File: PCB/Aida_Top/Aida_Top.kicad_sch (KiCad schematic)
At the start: 5 parts

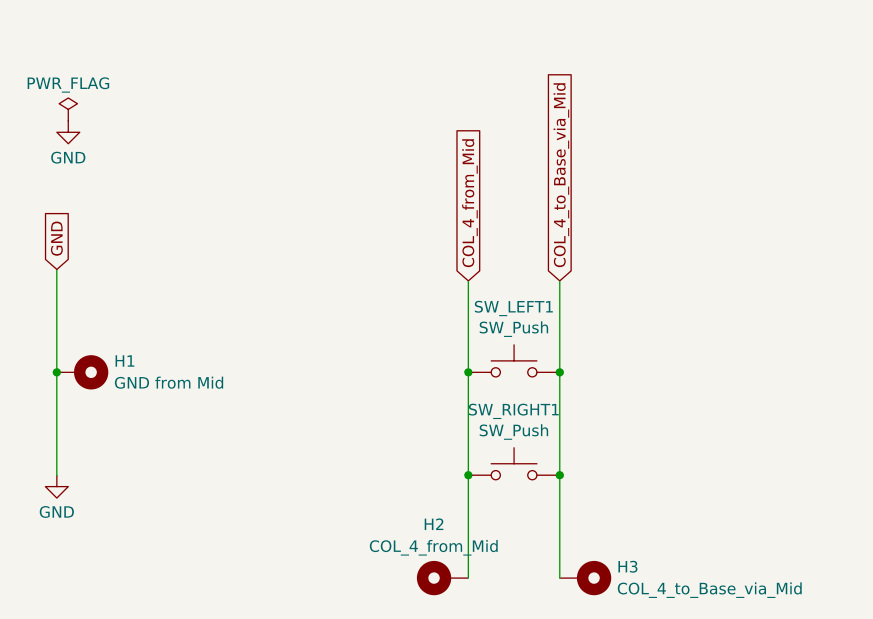
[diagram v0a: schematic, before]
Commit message: テストポイントを追加、配置した。
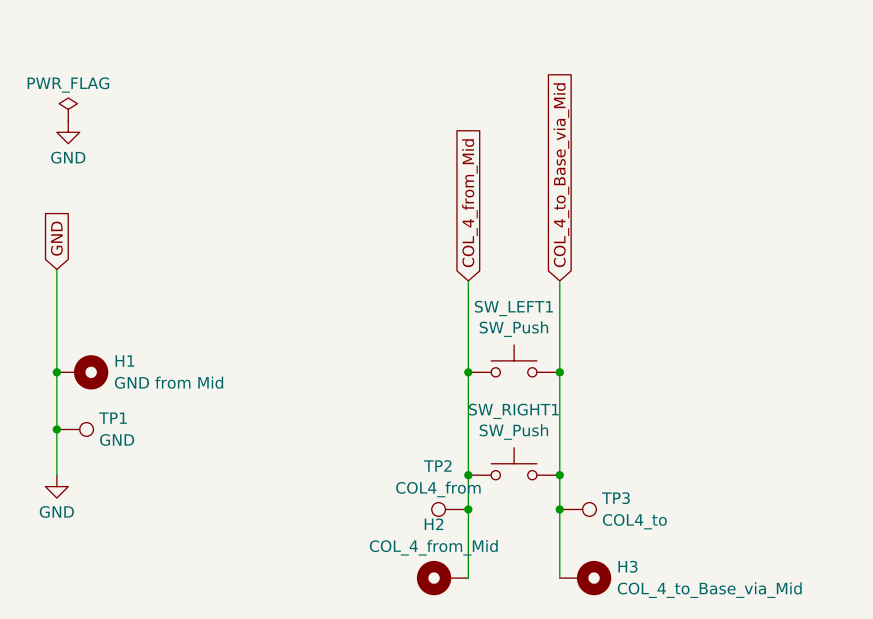
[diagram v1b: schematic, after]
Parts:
- added TP1: GND, Connector_PinHeader_2.00mm:PinHeader_1x01_P2.00mm_Vertical, symbol Connector:TestPoint
- added TP2: COL4_from, Connector_PinHeader_2.00mm:PinHeader_1x01_P2.00mm_Vertical, symbol Connector:TestPoint
- added TP3: COL4_to, Connector_PinHeader_2.00mm:PinHeader_1x01_P2.00mm_Vertical, symbol Connector:TestPoint
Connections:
- net COL_4_from_Mid: now also TP2.1
- net COL_4_to_Base_via_Mid: now also TP3.1
- net GND: now also TP1.1
